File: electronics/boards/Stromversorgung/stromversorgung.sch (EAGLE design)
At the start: 13 parts, among them IC2 NCP1117ST33T3G, J1 GROVE_CONNECTOR2.0_1X4, J2 GROVE_CONNECTOR2.0_1X4, J3 GROVE_CONNECTOR2.0_1X4, J4 GROVE_CONNECTOR2.0_1X4

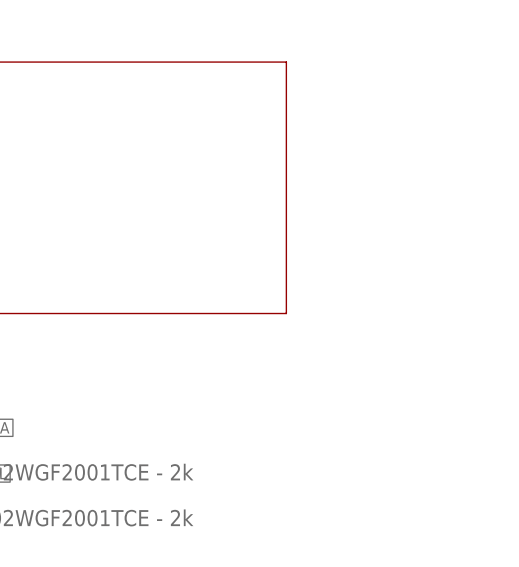
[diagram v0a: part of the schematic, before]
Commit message: Logo hinzugefügt
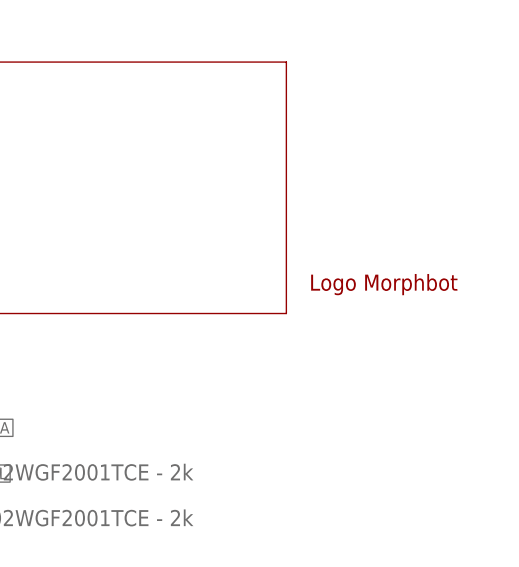
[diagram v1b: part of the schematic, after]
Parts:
- added U$1: LOGO_MORPHBOT5MM, topo-eng:LOGO_MORPHBOT5MM
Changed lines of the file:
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@@
 <layer number="104" name="Name" color="7" fill="1" visible="no" active="yes"/>
 <layer number="116" name="Patch_BOT" color="9" fill="4" visible="no" active="yes"/>
+<layer number="120" name="brd_placement_notes" color="7" fill="1" visible="yes" active="yes"/>
 <layer number="121" name="_tsilk" color="7" fill="1" visible="no" active="yes"/>
 <layer number="122" name="_bsilk" color="7" fill="1" visible="no" active="yes"/>
+<layer number="144" name="DrillLegend" color="7" fill="1" visible="yes" active="yes"/>
+<layer number="145" name="DrillLegend_01-16" color="7" fill="1" visible="yes" active="yes"/>
+<layer number="146" name="DrillLegend_01-20" color="7" fill="1" visible="yes" active="yes"/>
 <layer number="151" name="HeatSink" color="14" fill="1" visible="no" active="no"/>
+<layer number="198" name="BMP198" color="7" fill="1" visible="yes" active="yes"/>
+<layer number="199" name="Contour" color="7" fill="1" visible="yes" active="yes"/>
 <layer number="200" name="200bmp" color="1" fill="10" visible="no" active="no"/>
 <layer number="201" name="201bmp" color="2" fill="1" visible="no" active="no"/>
@@
 <layer number="207" name="207bmp" color="15" fill="10" visible="no" active="no"/>
 <layer number="208" name="208bmp" color="9" fill="10" visible="no" active="yes"/>
+<layer number="209" name="Route9Document" color="7" fill="1" visible="yes" active="yes"/>
+<layer number="210" name="Route10Document" color="7" fill="1" visible="yes" active="yes"/>
+<layer number="211" name="Route11Document" color="7" fill="1" visible="yes" active="yes"/>
+<layer number="212" name="Route12Document" color="7" fill="1" visible="yes" active="yes"/>
+<layer number="213" name="Route13Document" color="7" fill="1" visible="yes" active="yes"/>
+<layer number="214" name="Route14Document" color="7" fill="1" visible="yes" active="yes"/>
+<layer number="215" name="Route15Document" color="7" fill="1" visible="yes" active="yes"/>
+<layer number="216" name="BottomDocument" color="7" fill="1" visible="yes" active="yes"/>
+<layer number="220" name="DimensionDocument" color="7" fill="1" visible="yes" active="yes"/>
+<layer number="221" name="tPlaceDocument" color="7" fill="1" visible="yes" active="yes"/>
+<layer number="222" name="bPlaceDocument" color="7" fill="1" visible="yes" active="yes"/>
+<layer number="225" name="tNamesDocument" color="7" fill="1" visible="yes" active="yes"/>
+<layer number="226" name="bNamesDocument" color="7" fill="1" visible="yes" active="yes"/>
+<layer number="227" name="tValuesDocument" color="7" fill="1" visible="yes" active="yes"/>
+<layer number="228" name="bValuesDocument" color="7" fill="1" visible="yes" active="yes"/>
+<layer number="229" name="tStopDocument" color="7" fill="1" visible="yes" active="yes"/>
+<layer number="230" name="bStopDocument" color="7" fill="1" visible="yes" active="yes"/>
+<layer number="231" name="tCreamDocument" color="7" fill="1" visible="yes" active="yes"/>
+<layer number="232" name="bCreamDocument" color="7" fill="1" visible="yes" active="yes"/>
+<layer number="233" name="tFinishDocument" color="7" fill="1" visible="yes" active="yes"/>
+<layer number="234" name="bFinishDocument" color="7" fill="1" visible="yes" active="yes"/>
+<layer number="235" name="tGlueDocument" color="7" fill="1" visible="yes" active="yes"/>
+<layer number="236" name="bGlueDocument" color="7" fill="1" visible="yes" active="yes"/>
+<layer number="244" name="DrillsDocument" color="7" fill="1" visible="yes" active="yes"/>
+<layer number="245" name="HolesDocument" color="7" fill="1" visible="yes" active="yes"/>
+<layer number="246" name="MillingDocument" color="7" fill="1" visible="yes" active="yes"/>
+<layer number="247" name="MeasuresDocument" color="7" fill="1" visible="yes" active="yes"/>
 <layer number="250" name="Descript" color="3" fill="1" visible="no" active="no"/>
 <layer number="251" name="SMDround" color="12" fill="11" visible="no" active="no"/>
@@
 <part name="J3" library="morphbot" deviceset="GROVE_CONNECTOR" device="2.0_1X4" package3d_urn="urn:adsk.eagle:package:24855299/1"/>
 <part name="J4" library="morphbot" deviceset="GROVE_CONNECTOR" device="2.0_1X4" package3d_urn="urn:adsk.eagle:package:24855299/1"/>
+<part name="U$1" library="topo-eng" library_urn="urn:adsk.eagle:library:6646478" deviceset="LOGO_MORPHBOT" device="5MM"/>
 </parts>
 <sheets>
@@
 <attribute name="VALUE" x="17.018" y="110.744" size="1.27" layer="96" rot="R180"/>
 </instance>
+<instance part="U$1" gate="G$1" x="165.1" y="38.1" smashed="yes"/>
 </instances>
 <busses>

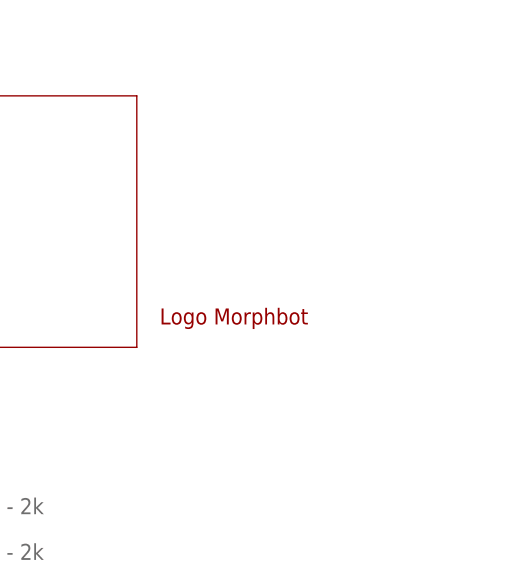
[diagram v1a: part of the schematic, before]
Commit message: Fiducials eingefügt
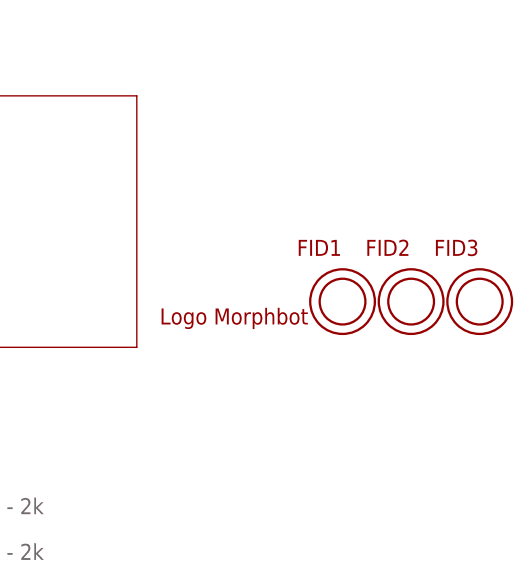
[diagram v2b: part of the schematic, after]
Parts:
- added FID1, FID2, FID3: OPEN-PNP-FIDUCIAL, topo-eng:OPEN-PNP-FIDUCIAL
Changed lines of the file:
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@@
 <part name="J4" library="morphbot" deviceset="GROVE_CONNECTOR" device="2.0_1X4" package3d_urn="urn:adsk.eagle:package:24855299/1"/>
 <part name="U$1" library="topo-eng" library_urn="urn:adsk.eagle:library:6646478" deviceset="LOGO_MORPHBOT" device="5MM"/>
+<part name="FID1" library="topo-eng" library_urn="urn:adsk.eagle:library:6646478" deviceset="OPEN-PNP-FIDUCIAL" device=""/>
+<part name="FID2" library="topo-eng" library_urn="urn:adsk.eagle:library:6646478" deviceset="OPEN-PNP-FIDUCIAL" device=""/>
+<part name="FID3" library="topo-eng" library_urn="urn:adsk.eagle:library:6646478" deviceset="OPEN-PNP-FIDUCIAL" device=""/>
 </parts>
 <sheets>
@@
 </instance>
 <instance part="U$1" gate="G$1" x="165.1" y="38.1" smashed="yes"/>
+<instance part="FID1" gate="FID$1" x="185.42" y="40.64" smashed="yes">
+<attribute name="NAME" x="180.34" y="45.72" size="1.778" layer="94"/>
+</instance>
+<instance part="FID2" gate="FID$1" x="193.04" y="40.64" smashed="yes">
+<attribute name="NAME" x="187.96" y="45.72" size="1.778" layer="94"/>
+</instance>
+<instance part="FID3" gate="FID$1" x="200.66" y="40.64" smashed="yes">
+<attribute name="NAME" x="195.58" y="45.72" size="1.778" layer="94"/>
+</instance>
 </instances>
 <busses>
